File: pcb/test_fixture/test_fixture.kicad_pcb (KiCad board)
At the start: 2 copper layers, 56 x 42.4 mm, 43 parts, among them J1 UART, J2 Power Input, J3 Conn_ARM_JTAG_SWD_10, P3.3V1 

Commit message: [pcb] finalized the fixture
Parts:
- added H10: Stand Mount, MountingHole:MountingHole_2.1mm, F.Cu at (142.9, 82.9)
- added H7: Stand Mount, MountingHole:MountingHole_2.1mm, F.Cu at (90.9, 83.1)
- added H8: Stand Mount, MountingHole:MountingHole_2.1mm, F.Cu at (142.7, 121.2)
- added H9: Stand Mount, MountingHole:MountingHole_2.1mm, F.Cu at (90.9, 121.2)
- added POGO19: pogo, dictofun:POGO_PIN, F.Cu at (137.0, 94.5)
- moved J4 2.22 mm to (110.7, 121.2)
- moved J6 1.66 mm to (136.4, 120.7)
- renumbered GND to J4, GND to J5, GND to J6
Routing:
- net /CHRG_IN: track 0.00 -> 9.36 mm
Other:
- board text added: "VBAT"
- board text removed: "VIN"
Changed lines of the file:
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@@
       (outputformat 1)
       (mirror false)
-      (drillshape 1)
+      (drillshape 0)
       (scaleselection 1)
-      (outputdirectory "")
+      (outputdirectory "../out/v1.2_fixture/gerbers/")
     )
   )
@@
   (net 21 "Net-(J3-Pad8)")
   (net 22 "Net-(J3-Pad3)")
+  (net 23 "/CHRG_IN")
   (footprint "MountingHole:MountingHole_2.1mm" (layer "F.Cu")
     (at 99.06 92.837)
@@
   )
   (footprint "dictofun:POGO_PIN" (layer "F.Cu")
+    (at 137.033 94.488)
+    (property "Sheetfile" "test_fixture.kicad_sch")
+    (property "Sheetname" "")
+    (attr through_hole)
+    (fp_text reference "POGO19" (at 0 -2.54 unlocked) (layer "F.SilkS") hide
+      (effects (font (size 1 1) (thickness 0.15)))
+    )
+    (fp_text value "pogo" (at 0 2.54 unlocked) (layer "F.Fab") hide
+      (effects (font (size 1 1) (thickness 0.15)))
+    )
+    (pad "1" thru_hole circle (at 0 0) (size 1.27 1.27) (drill 0.4826) (layers *.Cu *.Mask)
+      (net 23 "/CHRG_IN") (pinfunction "Pin_1") (pintype "passive"))
+  )
+  (footprint "dictofun:POGO_PIN" (layer "F.Cu")
     (at 106.045 98.171)
     (property "Sheetfile" "test_fixture.kicad_sch")
@@
       (net 14 "/SPI_CLK") (pinfunction "Pin_1") (pintype "passive"))
   )
+  (footprint "MountingHole:MountingHole_2.1mm" (layer "F.Cu")
+    (at 90.932 83.058)
+    (descr "Mounting Hole 2.1mm, no annular")
+    (tags "mounting hole 2.1mm no annular")
+    (property "Sheetfile" "test_fixture.kicad_sch")
+    (property "Sheetname" "")
+    (attr exclude_from_pos_files)
+    (fp_text reference "H7" (at 0 -3.2) (layer "F.SilkS") hide
+      (effects (font (size 1 1) (thickness 0.15)))
+    )
+    (fp_text value "Stand Mount" (at 0 3.2) (layer "F.Fab")
+      (effects (font (size 1 1) (thickness 0.15)))
+    )
+    (fp_text user "${REFERENCE}" (at 0 0) (layer "F.Fab")
+      (effects (font (size 1 1) (thickness 0.15)))
+    )
+    (fp_circle (center 0 0) (end 2.1 0) (layer "Cmts.User") (width 0.15) (fill none))
+    (fp_circle (center 0 0) (end 2.35 0) (layer "F.CrtYd") (width 0.05) (fill none))
+    (pad "" np_thru_hole circle (at 0 0) (size 2.1 2.1) (drill 2.1) (layers *.Cu *.Mask))
+  )
   (footprint "Connector_PinHeader_2.54mm:PinHeader_1x03_P2.54mm_Vertical" (layer "F.Cu")
     (at 99.426 116.967 -90)
@@
       (net 15 "/PDM_CLK") (pinfunction "1") (pintype "passive"))
   )
+  (footprint "MountingHole:MountingHole_2.1mm" (layer "F.Cu")
+    (at 142.748 121.158)
+    (descr "Mounting Hole 2.1mm, no annular")
+    (tags "mounting hole 2.1mm no annular")
+    (property "Sheetfile" "test_fixture.kicad_sch")
+    (property "Sheetname" "")
+    (attr exclude_from_pos_files)
+    (fp_text reference "H8" (at 0 -3.2) (layer "F.SilkS") hide
+      (effects (font (size 1 1) (thickness 0.15)))
+    )
+    (fp_text value "Stand Mount" (at 0 3.2) (layer "F.Fab")
+      (effects (font (size 1 1) (thickness 0.15)))
+    )
+    (fp_text user "${REFERENCE}" (at 0 0) (layer "F.Fab")
+      (effects (font (size 1 1) (thickness 0.15)))
+    )
+    (fp_circle (center 0 0) (end 2.1 0) (layer "Cmts.User") (width 0.15) (fill none))
+    (fp_circle (center 0 0) (end 2.35 0) (layer "F.CrtYd") (width 0.05) (fill none))
+    (pad "" np_thru_hole circle (at 0 0) (size 2.1 2.1) (drill 2.1) (layers *.Cu *.Mask))
+  )
+  (footprint "MountingHole:MountingHole_2.1mm" (layer "F.Cu")
+    (at 90.932 121.158)
+    (descr "Mounting Hole 2.1mm, no annular")
+    (tags "mounting hole 2.1mm no annular")
+    (property "Sheetfile" "test_fixture.kicad_sch")
+    (property "Sheetname" "")
+    (attr exclude_from_pos_files)
+    (fp_text reference "H9" (at 0 -3.2) (layer "F.SilkS") hide
+      (effects (font (size 1 1) (thickness 0.15)))
+    )
+    (fp_text value "Stand Mount" (at 0 3.2) (layer "F.Fab")
+      (effects (font (size 1 1) (thickness 0.15)))
+    )
+    (fp_text user "${REFERENCE}" (at 0 0) (layer "F.Fab")
+      (effects (font (size 1 1) (thickness 0.15)))
+    )
+    (fp_circle (center 0 0) (end 2.1 0) (layer "Cmts.User") (width 0.15) (fill none))
+    (fp_circle (center 0 0) (end 2.35 0) (layer "F.CrtYd") (width 0.05) (fill none))
+    (pad "" np_thru_hole circle (at 0 0) (size 2.1 2.1) (drill 2.1) (layers *.Cu *.Mask))
+  )
   (footprint "Connector_PinSocket_2.54mm:PinSocket_1x01_P2.54mm_Vertical" (layer "F.Cu")
-    (at 138.049 120.523 90)
+    (at 136.398 120.65 90)
     (descr "Through hole straight socket strip, 1x01, 2.54mm pitch, single row (from Kicad 4.0.7), script generated")
     (tags "Through hole socket strip THT 1x01 2.54mm single row")
@@
     (property "Sheetname" "")
     (attr through_hole)
-    (fp_text reference "GND" (at 0 2.794 90) (layer "F.SilkS")
+    (fp_text reference "J6" (at 0 2.794 90) (layer "F.SilkS") hide
       (effects (font (size 1 1) (thickness 0.15)))
     )
@@
       (net 13 "/SPI_CS") (pinfunction "1") (pintype "passive"))
   )
+  (footprint "MountingHole:MountingHole_2.1mm" (layer "F.Cu")
+    (at 142.875 82.931)
+    (descr "Mounting Hole 2.1mm, no annular")
+    (tags "mounting hole 2.1mm no annular")
+    (property "Sheetfile" "test_fixture.kicad_sch")
+    (property "Sheetname" "")
+    (attr exclude_from_pos_files)
+    (fp_text reference "H10" (at 0 -3.2) (layer "F.SilkS") hide
+      (effects (font (size 1 1) (thickness 0.15)))
+    )
+    (fp_text value "Stand Mount" (at 0 3.2) (layer "F.Fab")
+      (effects (font (size 1 1) (thickness 0.15)))
+    )
+    (fp_text user "${REFERENCE}" (at 0 0) (layer "F.Fab")
+      (effects (font (size 1 1) (thickness 0.15)))
+    )
+    (fp_circle (center 0 0) (end 2.1 0) (layer "Cmts.User") (width 0.15) (fill none))
+    (fp_circle (center 0 0) (end 2.35 0) (layer "F.CrtYd") (width 0.05) (fill none))
+    (pad "" np_thru_hole circle (at 0 0) (size 2.1 2.1) (drill 2.1) (layers *.Cu *.Mask))
+  )
   (footprint "dictofun:POGO_PIN" (layer "F.Cu")
     (at 114.173 87.122)
@@
     (property "Sheetname" "")
     (attr through_hole)
-    (fp_text reference "GND" (at 0 3.048 90) (layer "F.SilkS")
+    (fp_text reference "J5" (at 0 3.048 90) (layer "F.SilkS") hide
       (effects (font (size 1 1) (thickness 0.15)))
     )
@@
   )
   (footprint "Connector_PinSocket_2.54mm:PinSocket_1x01_P2.54mm_Vertical" (layer "F.Cu")
-    (at 108.585 121.666 90)
+    (at 110.744 121.158 90)
     (descr "Through hole straight socket strip, 1x01, 2.54mm pitch, single row (from Kicad 4.0.7), script generated")
     (tags "Through hole socket strip THT 1x01 2.54mm single row")
@@
     (property "Sheetname" "")
     (attr through_hole)
-    (fp_text reference "GND" (at 0.381 2.54 90) (layer "F.SilkS")
+    (fp_text reference "J4" (at 0.381 2.54 90) (layer "F.SilkS") hide
       (effects (font (size 1 1) (thickness 0.15)))
     )
@@
   (gr_line (start 144.78 81.026) (end 88.773 81.026) (layer "Edge.Cuts") (width 0.1))
   (gr_line (start 88.773 81.026) (end 88.773 123.444) (layer "Edge.Cuts") (width 0.1))
-  (gr_text "Dictofun-1.2-Test" (at 132.969 83.312) (layer "F.Cu")
+  (gr_text "Dictofun-1.2-Test" (at 116.84 83.566) (layer "F.Cu")
     (effects (font (size 1.5 1.5) (thickness 0.3)))
   )
@@
     (effects (font (size 1.5 1.5) (thickness 0.3)))
   )
-  (gr_text "VIN" (at 138.43 106.68) (layer "F.Cu")
+  (gr_text "VBAT" (at 138.049 106.68) (layer "F.Cu")
     (effects (font (size 1.5 1.5) (thickness 0.3)))
   )
+  (gr_text "https://github.com/rundb/dictofun" (at 121.158 114.935) (layer "B.Cu")
+    (effects (font (size 1.5 1.5) (thickness 0.3) italic) (justify mirror))
+  )
+  (gr_text "https://github.com/rundb/dictofun" (at 121.158 114.935) (layer "B.SilkS")
+    (effects (font (size 1.5 1.5) (thickness 0.3) italic) (justify mirror))
+  )
   (gr_text "TX" (at 97.155 119.38 90) (layer "F.SilkS")
     (effects (font (size 1 1) (thickness 0.15)))
   )
+  (gr_text "GND" (at 138.684 120.65 90) (layer "F.SilkS")
+    (effects (font (size 1 1) (thickness 0.15)))
+  )
   (gr_text "GND" (at 138.557 109.347) (layer "F.SilkS")
     (effects (font (size 1.5 1.5) (thickness 0.3)))
   )
-  (gr_text "https://github.com/rundb/dictofun" (at 103.759 83.058) (layer "F.SilkS")
-    (effects (font (size 1 1) (thickness 0.15) italic))
+  (gr_text "GND" (at 131.445 120.777 90) (layer "F.SilkS")
+    (effects (font (size 1 1) (thickness 0.15)))
+  )
+  (gr_text "GND" (at 113.157 121.158 90) (layer "F.SilkS")
+    (effects (font (size 1 1) (thickness 0.15)))
   )
   (gr_text "GND" (at 99.695 119.634 90) (layer "F.SilkS")
     (effects (font (size 1 1) (thickness 0.15)))
   )
-  (gr_text "Dictofun-1.2-Test" (at 132.969 83.312) (layer "F.SilkS")
+  (gr_text "Dictofun-1.2-Test" (at 116.84 83.566) (layer "F.SilkS")
     (effects (font (size 1.5 1.5) (thickness 0.3)))
   )
-  (gr_text "VIN" (at 138.43 106.68) (layer "F.SilkS")
+  (gr_text "VBAT" (at 138.049 106.68) (layer "F.SilkS")
     (effects (font (size 1.5 1.5) (thickness 0.3)))
   )
@@
   (segment (start 101.727 97.155) (end 100.33 95.758) (width 0.25) (layer "F.Cu") (net 22))
   (segment (start 98.47 104.775) (end 100.584 104.775) (width 0.25) (layer "F.Cu") (net 22))
+  (segment (start 137.033 94.488) (end 139.7 97.155) (width 0.25) (layer "F.Cu") (net 23))
+  (segment (start 139.7 97.155) (end 139.7 102.743) (width 0.25) (layer "F.Cu") (net 23))
   (zone (net 1) (net_name "GNDD") (layers F&B.Cu) (hatch edge 0.508)
     (connect_pads (clearance 0.508))

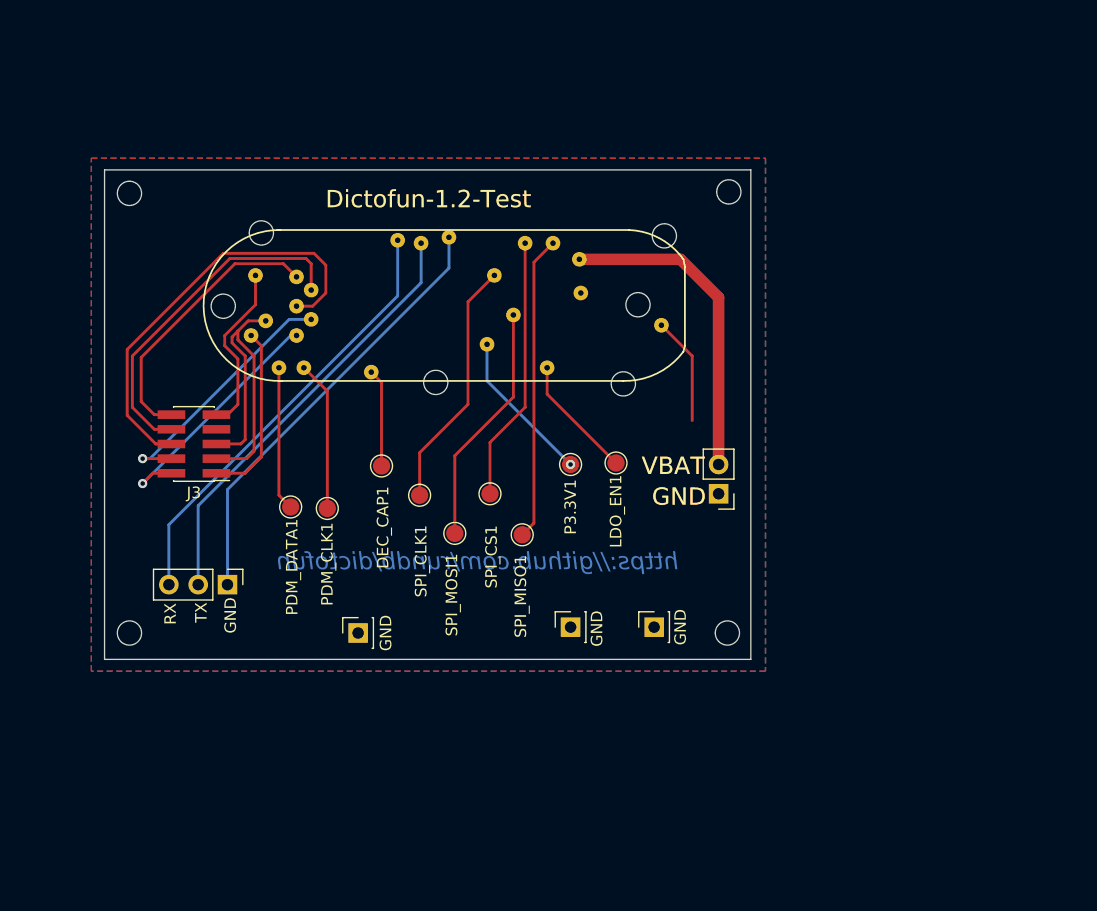
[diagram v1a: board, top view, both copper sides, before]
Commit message: [pcb] version 1.3 (#75)
Changes:
    LDO voltage regulator replaced with DC-DC (expected increase in efficiency)
    added small-footprint RTC chip
    analog latch for regulator EN pin replaced with a digital flip-flop

Fixture:
    added Raspberry Pico to the PCB
    added current measurement setup
    planning to reduce hardware in use to a single PCB
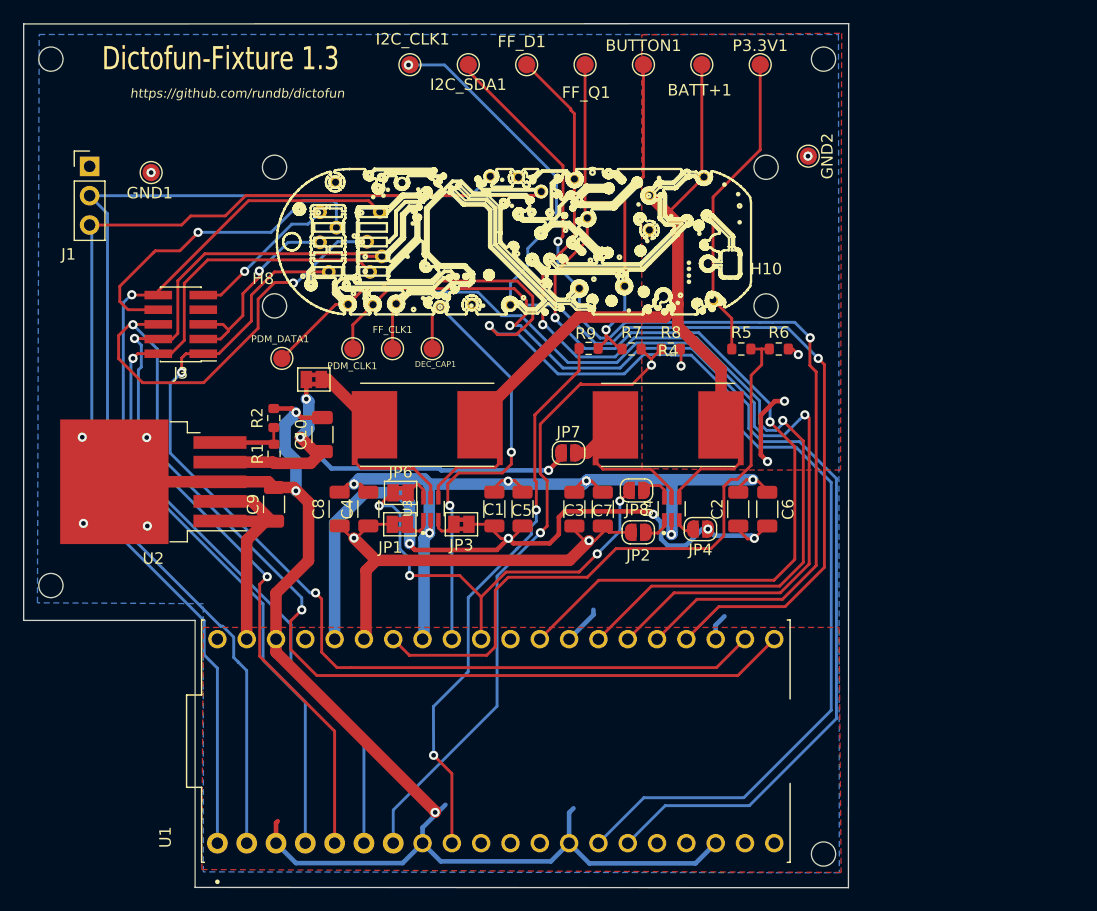
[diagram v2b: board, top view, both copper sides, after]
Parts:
- removed H1, H2: PCB Mount, MountingHole:MountingHole_2.1mm
- removed J2: Power Input, Connector_PinHeader_2.54mm:PinHeader_1x02_P2.54mm_Vertical
- removed J4: GND, Connector_PinSocket_2.54mm:PinSocket_1x01_P2.54mm_Vertical
- removed LDO_EN1, SPI_CLK1, SPI_CS1, SPI_MISO1, SPI_MOSI1: , TestPoint:TestPoint_Pad_D1.5mm
- removed POGO9: pogo, dictofun:POGO_PIN
- added BATT+1: , TestPoint:TestPoint_Pad_D1.5mm, F.Cu at (140.5, 71.9)
- added BUTTON1: , TestPoint:TestPoint_Pad_D1.5mm, F.Cu at (135.5, 71.9)
- added C1: 1u, Resistor_SMD:R_1206_3216Metric, F.Cu at (122.6, 110.4)
- added C10: 22u, Capacitor_SMD:C_1206_3216Metric, F.Cu at (107.7, 104.0)
- added C2: 1u, Resistor_SMD:R_1206_3216Metric, F.Cu at (143.7, 110.4)
- added C3: 1u, Resistor_SMD:R_1206_3216Metric, F.Cu at (129.5, 110.4)
- added C4: 1u, Resistor_SMD:R_1206_3216Metric, F.Cu at (111.6, 110.4)
- added C5: 100n, Resistor_SMD:R_1206_3216Metric, F.Cu at (125.0, 110.4)
- added C6: 100n, Resistor_SMD:R_1206_3216Metric, F.Cu at (146.2, 110.4)
- added C7: 100n, Resistor_SMD:R_1206_3216Metric, F.Cu at (132.0, 110.4)
- added C8: 100n, Resistor_SMD:R_1206_3216Metric, F.Cu at (109.1, 110.4)
- added C9: 10u, Resistor_SMD:R_1206_3216Metric, F.Cu at (103.5, 110.0)
- added FF_CLK1: , TestPoint:TestPoint_Pad_D1.5mm, F.Cu at (113.7, 96.5)
- added FF_D1: , TestPoint:TestPoint_Pad_D1.5mm, F.Cu at (125.4, 71.9)
- added FF_Q1: , TestPoint:TestPoint_Pad_D1.5mm, F.Cu at (130.4, 71.9)
- added GND1: , TestPoint:TestPoint_Pad_D1.5mm, F.Cu at (92.8, 81.3)
- added GND2: , TestPoint:TestPoint_Pad_D1.5mm, F.Cu at (149.8, 79.8)
- added I2C_CLK1: , TestPoint:TestPoint_Pad_D1.5mm, F.Cu at (115.2, 71.9)
- added I2C_SDA1: , TestPoint:TestPoint_Pad_D1.5mm, F.Cu at (120.3, 71.9)
- added JP1: Jumper_2_Bridged, Jumper:SolderJumper-2_P1.3mm_Bridged2Bar_Pad1.0x1.5mm, F.Cu at (114.4, 111.7)
- added JP2: Jumper_2_Open, Jumper:SolderJumper-2_P1.3mm_Open_RoundedPad1.0x1.5mm, F.Cu at (135.0, 112.4)
- added JP3: Jumper_2_Bridged, Jumper:SolderJumper-2_P1.3mm_Bridged2Bar_Pad1.0x1.5mm, F.Cu at (119.7, 111.7)
- added JP4: Jumper_2_Open, Jumper:SolderJumper-2_P1.3mm_Open_RoundedPad1.0x1.5mm, F.Cu at (140.4, 112.2)
- added JP5: Jumper_2_Bridged, Jumper:SolderJumper-2_P1.3mm_Bridged2Bar_Pad1.0x1.5mm, F.Cu at (106.9, 99.2)
- added JP6: Jumper_2_Bridged, Jumper:SolderJumper-2_P1.3mm_Bridged2Bar_Pad1.0x1.5mm, F.Cu at (114.4, 109.0)
- added JP7: Jumper_2_Open, Jumper:SolderJumper-2_P1.3mm_Open_RoundedPad1.0x1.5mm, F.Cu at (129.0, 105.5)
- added JP8: Jumper_2_Open, Jumper:SolderJumper-2_P1.3mm_Open_RoundedPad1.0x1.5mm, F.Cu at (134.9, 108.8)
- added POGO24: pogo, fixture:POGO, F.Cu at (112.0, 92.7)
- added POGO25: pogo, fixture:POGO, F.Cu at (109.9, 92.7)
- added R1: 415, Resistor_SMD:R_0603_1608Metric, F.Cu at (103.5, 105.6)
- added R2: 187, Resistor_SMD:R_0603_1608Metric, F.Cu at (103.4, 102.5)
- added R3: 0.04, Resistor_SMD:R_Shunt_Vishay_WSR2_WSR3_KelvinConnection, F.Cu at (116.7, 103.4)
- added R4: 0.01, Resistor_SMD:R_Shunt_Vishay_WSR2_WSR3_KelvinConnection, F.Cu at (137.6, 103.4)
- added R5: 100K, Resistor_SMD:R_0603_1608Metric, F.Cu at (144.0, 96.5)
- added R6: 100K, Resistor_SMD:R_0603_1608Metric, F.Cu at (147.2, 96.5)
- added R7: 200K, Resistor_SMD:R_0603_1608Metric, F.Cu at (134.4, 96.5)
- added R8: 300K, Resistor_SMD:R_0603_1608Metric, F.Cu at (137.8, 96.5)
- added R9: 1K, Resistor_SMD:R_0603_1608Metric, F.Cu at (130.7, 96.5)
- added U1: SC0915, fixture:MODULE_SC0915, F.Cu at (122.7, 130.5)
- added U2: MIC29302WU, Package_TO_SOT_SMD:TO-263-5_TabPin3, F.Cu at (93.0, 108.1)
- added U3: INA186A5IDCKR, fixture:SOT65P210X110-6N, F.Cu at (117.0, 110.4)
- added U4: INA186A5IDCKR, fixture:SOT65P210X110-6N, F.Cu at (137.9, 110.4)
- J5, J6: footprint Connector_PinSocket_2.54mm:PinSocket_1x01_P2.54mm_Vertical -> fixture:POGO
- POGO1, POGO10, POGO11, POGO12, POGO13, POGO14, POGO15, POGO16, POGO17, POGO18, POGO19, POGO2, POGO20, POGO21, POGO22, POGO23, POGO3, POGO4, POGO5, POGO6, POGO7, POGO8: footprint dictofun:POGO_PIN -> fixture:POGO
- moved H9 68.4 mm to (146.1, 80.8)
- moved H8 48.4 mm to (103.5, 92.8)
- moved H6 44.3 mm to (151.1, 140.3)
- moved P3.3V1 38.3 mm to (145.6, 71.9)
- moved J1 38.2 mm to (87.5, 80.7), turned to 0 degrees
- moved H4 37.7 mm to (84.1, 117.0)
- moved J6 34.4 mm to (136.0, 86.2), turned to 0 degrees
- moved J5 29.2 mm to (120.6, 92.7), turned to 0 degrees
- moved POGO12 26.9 mm to (129.9, 91.3)
- moved H3 23.7 mm to (84.1, 71.4)
- moved H5 20.6 mm to (151.1, 71.4)
- moved POGO16 20.0 mm to (141.5, 92.3)
- moved POGO11 18.7 mm to (124.0, 92.7)
- moved PDM_CLK1 14.0 mm to (110.3, 96.5)
- moved POGO15 13.4 mm to (130.6, 85.2)
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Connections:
- J1 pad 1: GNDD -> GND
- J3 pad 3: Net-(J3-Pad3) -> GND
- J3 pad 5: Net-(J3-Pad3) -> GND
- J3 pad 9: Net-(J3-Pad9) -> GND
- J5 pad 1: GNDD -> GND
- J6 pad 1: GNDD -> GND
- POGO10 pad 1: /SPI_CLK -> /FF_CLK
- POGO11 pad 1: /PDM_CLK -> /I2C_CLK
- POGO12 pad 1: /PDM_DATA -> /I2C_DATA
- POGO13 pad 1: /POWER_VBAT -> /BATT+
- POGO14 pad 1: GNDD -> GND
- POGO15 pad 1: /LDO_EN -> /FF_Q
- POGO19 pad 1: /CHRG_IN -> /BATT+
- POGO3 pad 1: Net-(J3-Pad3) -> GND
- POGO4 pad 1: Net-(J3-Pad9) -> GND
- POGO6 pad 1: GNDD -> GND
- POGO7 pad 1: /SPI_MOSI -> /BUTTON
- POGO8 pad 1: /SPI_MISO -> /FF_D
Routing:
- net GND: track 0.00 -> 161.0 mm, vias 0 -> 15
- net /PDM_DATA: track 12.5 -> 114.3 mm, vias 0 -> 1
- net /I2C_CLK: track 0.00 -> 92.3 mm, vias 0 -> 2
- net /PDM_CLK: track 13.0 -> 101.6 mm, vias 0 -> 1
- net /FF_D: track 0.00 -> 86.6 mm, vias 0 -> 2
- net /FF_Q: track 0.00 -> 85.5 mm, vias 0 -> 2
- net /I2C_DATA: track 0.00 -> 84.9 mm, vias 0 -> 2
- net /FF_CLK: track 0.00 -> 79.5 mm, vias 0 -> 1
- net /SWO: track 37.1 -> 113.7 mm, vias 0 -> 3
- net /BATT+: track 0.00 -> 72.9 mm
- net /VTREF: track 15.4 -> 87.2 mm, vias 0 -> 2
- net GNDA: track 0.00 -> 70.0 mm, vias 0 -> 6
- net +3.3V: track 0.00 -> 66.9 mm, vias 0 -> 5
- net /UART_RX: track 38.1 -> 98.5 mm
- net /UART_TX: track 37.6 -> 97.4 mm
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- added copper zone on B.Cu, net GND
- added copper zone on F.Cu, net GND
- removed copper zone on B.Cu, net GNDD
- removed copper zone on F.Cu, net GNDD
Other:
- board size 56 x 42.4 mm -> 71.5 x 74.9 mm
- board text added: "Dictofun-Fixture 1.3"
- board text removed: "Dictofun-1.2-Test"
- board text removed: "GND"
- board text removed: "RX"
- board text removed: "TX"
- board text removed: "VBAT"
